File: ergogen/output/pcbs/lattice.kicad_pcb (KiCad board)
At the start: 2 copper layers, 102 x 76.5 mm, 70 parts

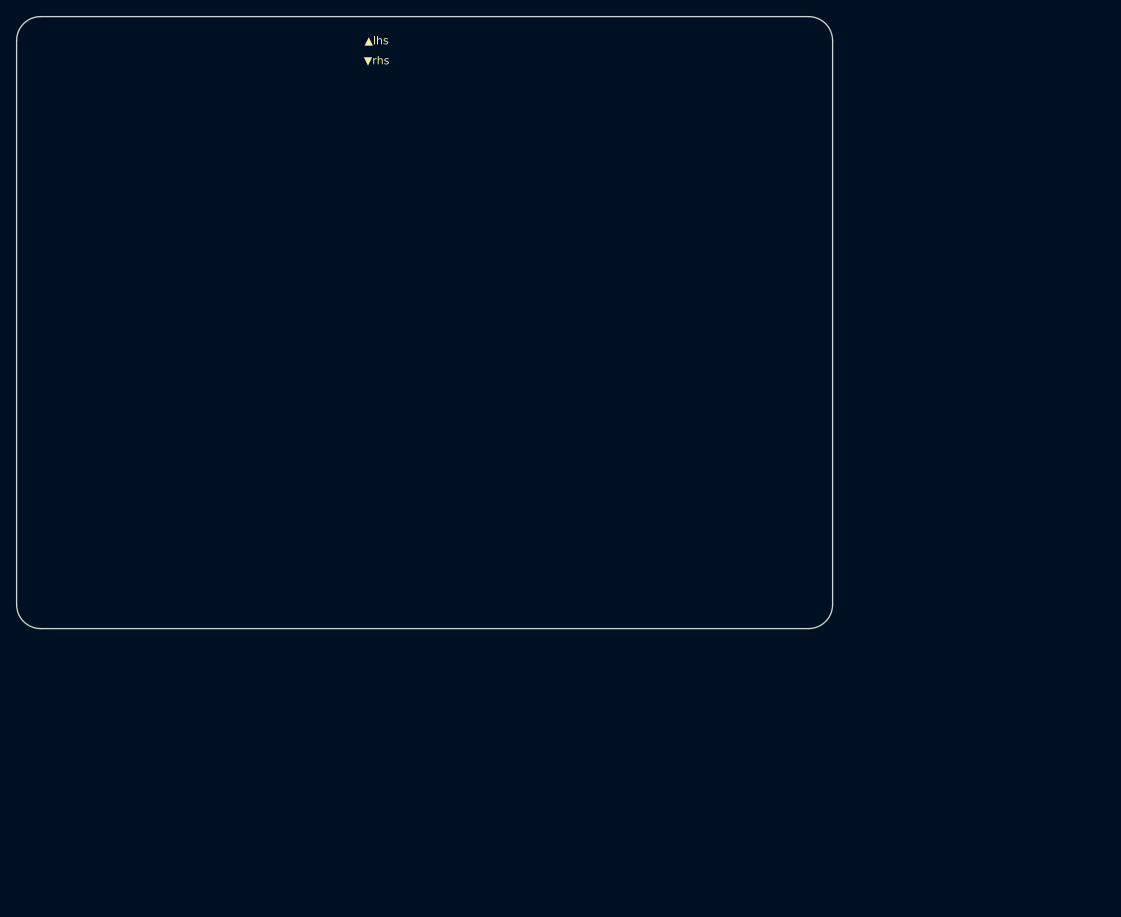
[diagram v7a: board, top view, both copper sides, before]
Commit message: jumper label as footprint
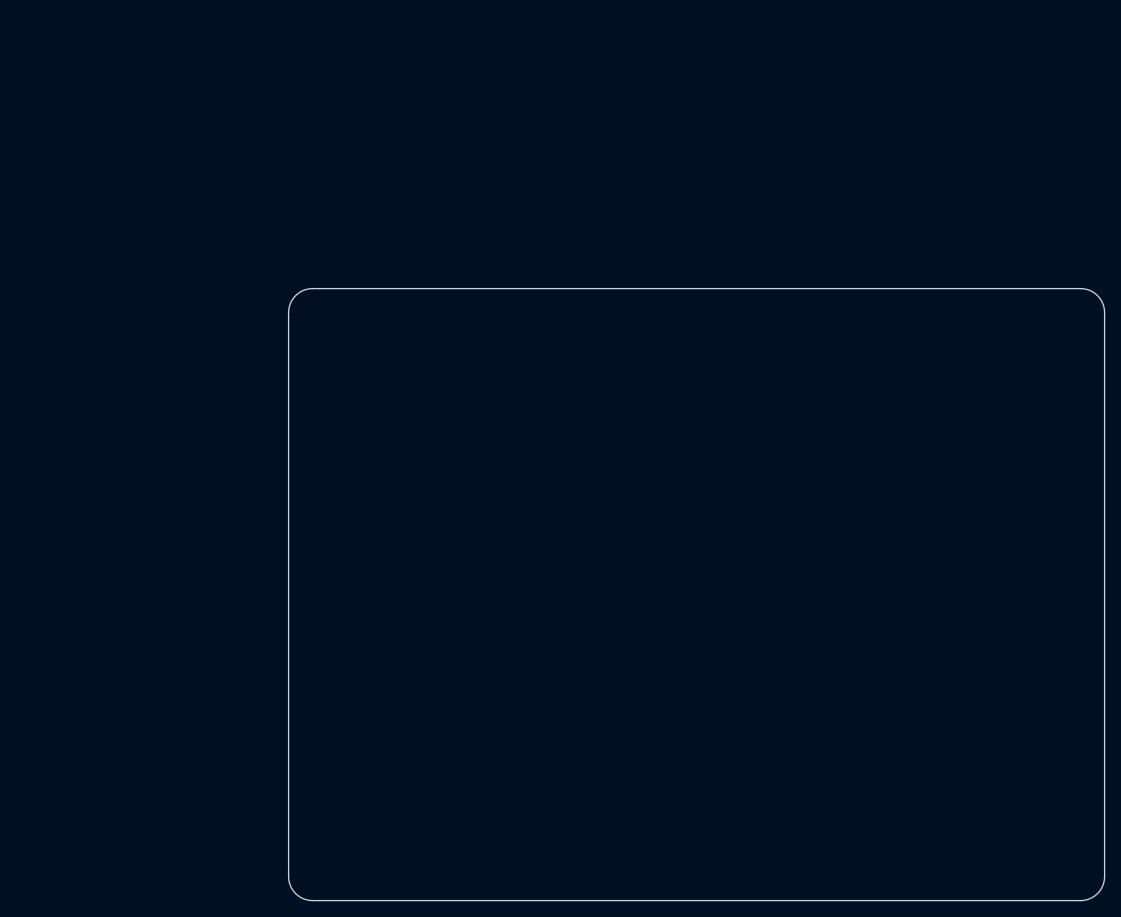
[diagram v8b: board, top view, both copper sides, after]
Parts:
- added L1: , SolderJumperLabel, F.Cu at (146.2, 72.0)
- moved B1 48.1 mm to (178.5, 72.0)
- moved C1 48.1 mm to (170.0, 70.0)
- moved C2 48.1 mm to (170.0, 72.0)
- moved D1 48.1 mm to (119.0, 131.2)
- moved D10 48.1 mm to (153.0, 114.2)
- moved D11 48.1 mm to (153.0, 97.2)
- moved D12 48.1 mm to (153.0, 80.2)
- moved D13 48.1 mm to (170.0, 131.2)
- moved D14 48.1 mm to (170.0, 114.2)
- moved D15 48.1 mm to (170.0, 97.2)
- moved D16 48.1 mm to (170.0, 80.2)
- moved D17 48.1 mm to (187.0, 131.2)
- moved D18 48.1 mm to (187.0, 114.2)
- moved D19 48.1 mm to (187.0, 97.2)
- moved D2 48.1 mm to (119.0, 114.2)
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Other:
- board text removed: "▲lhs"
- board text removed: "▼rhs"
